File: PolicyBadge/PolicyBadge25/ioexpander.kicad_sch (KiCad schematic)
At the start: 25 parts, among them Q1 2N7002, U10 YX-SMD5020, U9 TCA9555PWR

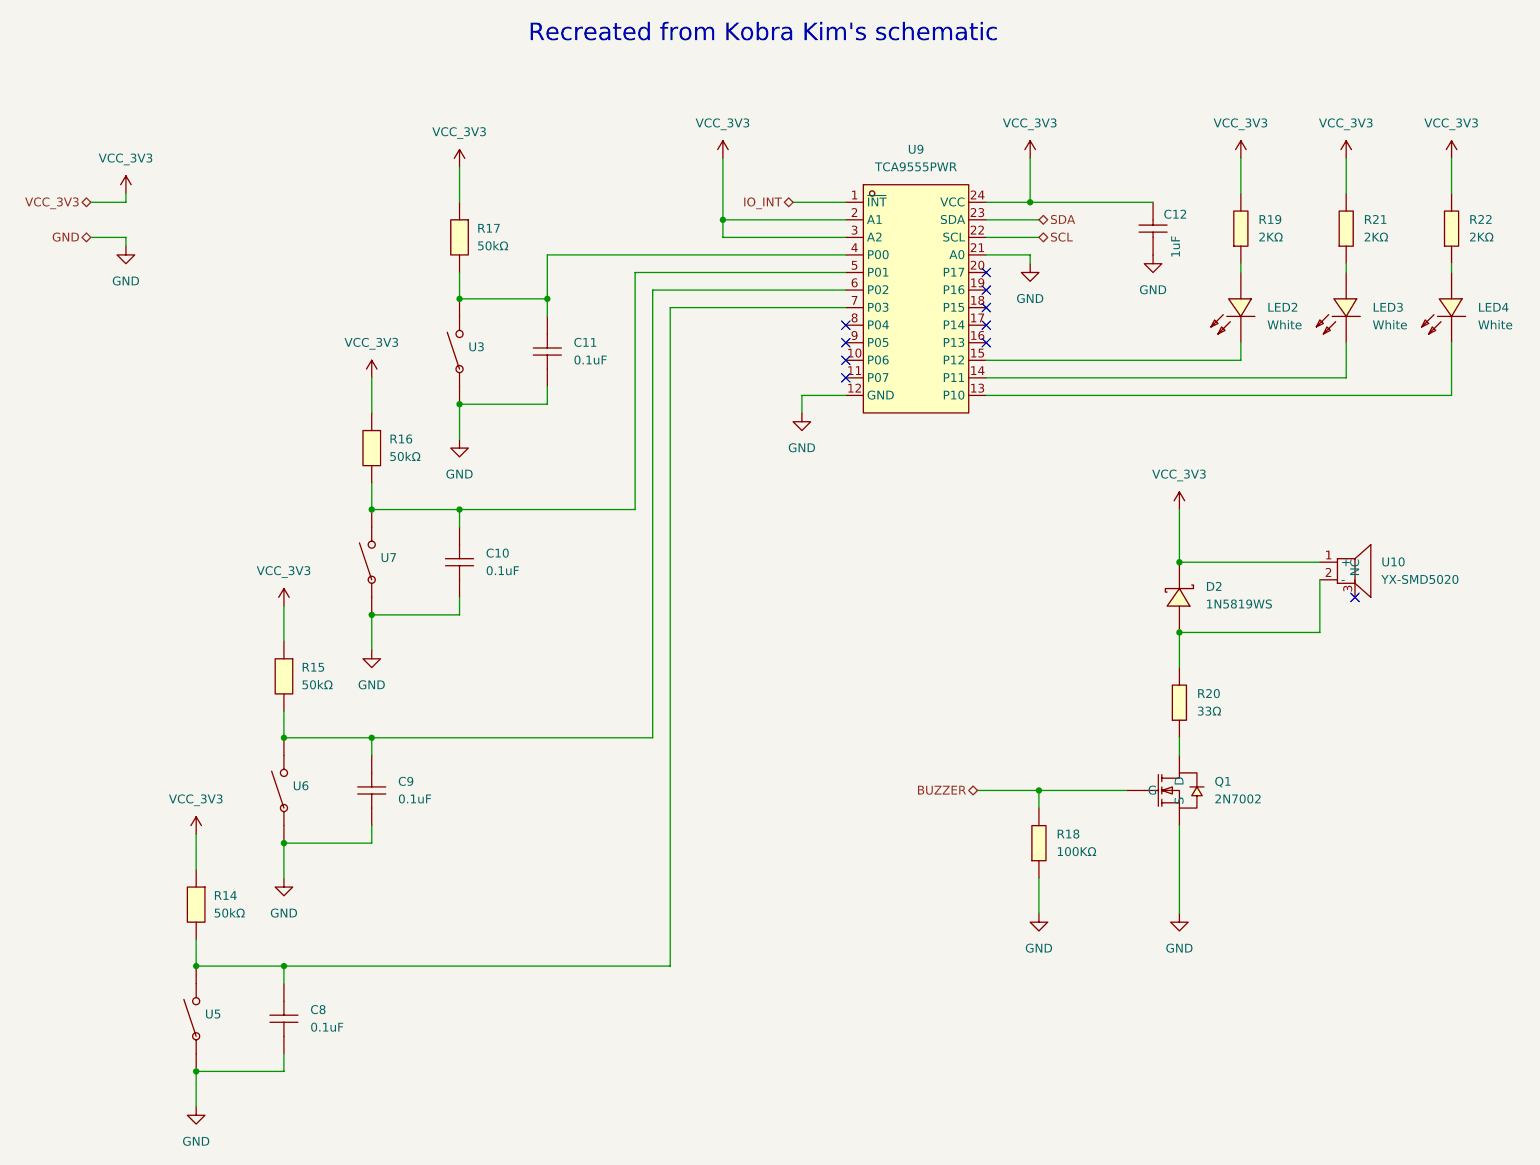
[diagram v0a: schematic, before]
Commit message: Lots of changes, laying out board for board shape
Updated switches
Added headers for XAIO
Fixed Batt Connector polarity
10K pullup on int
Batt monitor resistor divider
Fix buzzer trace
XAIO footprint spacing
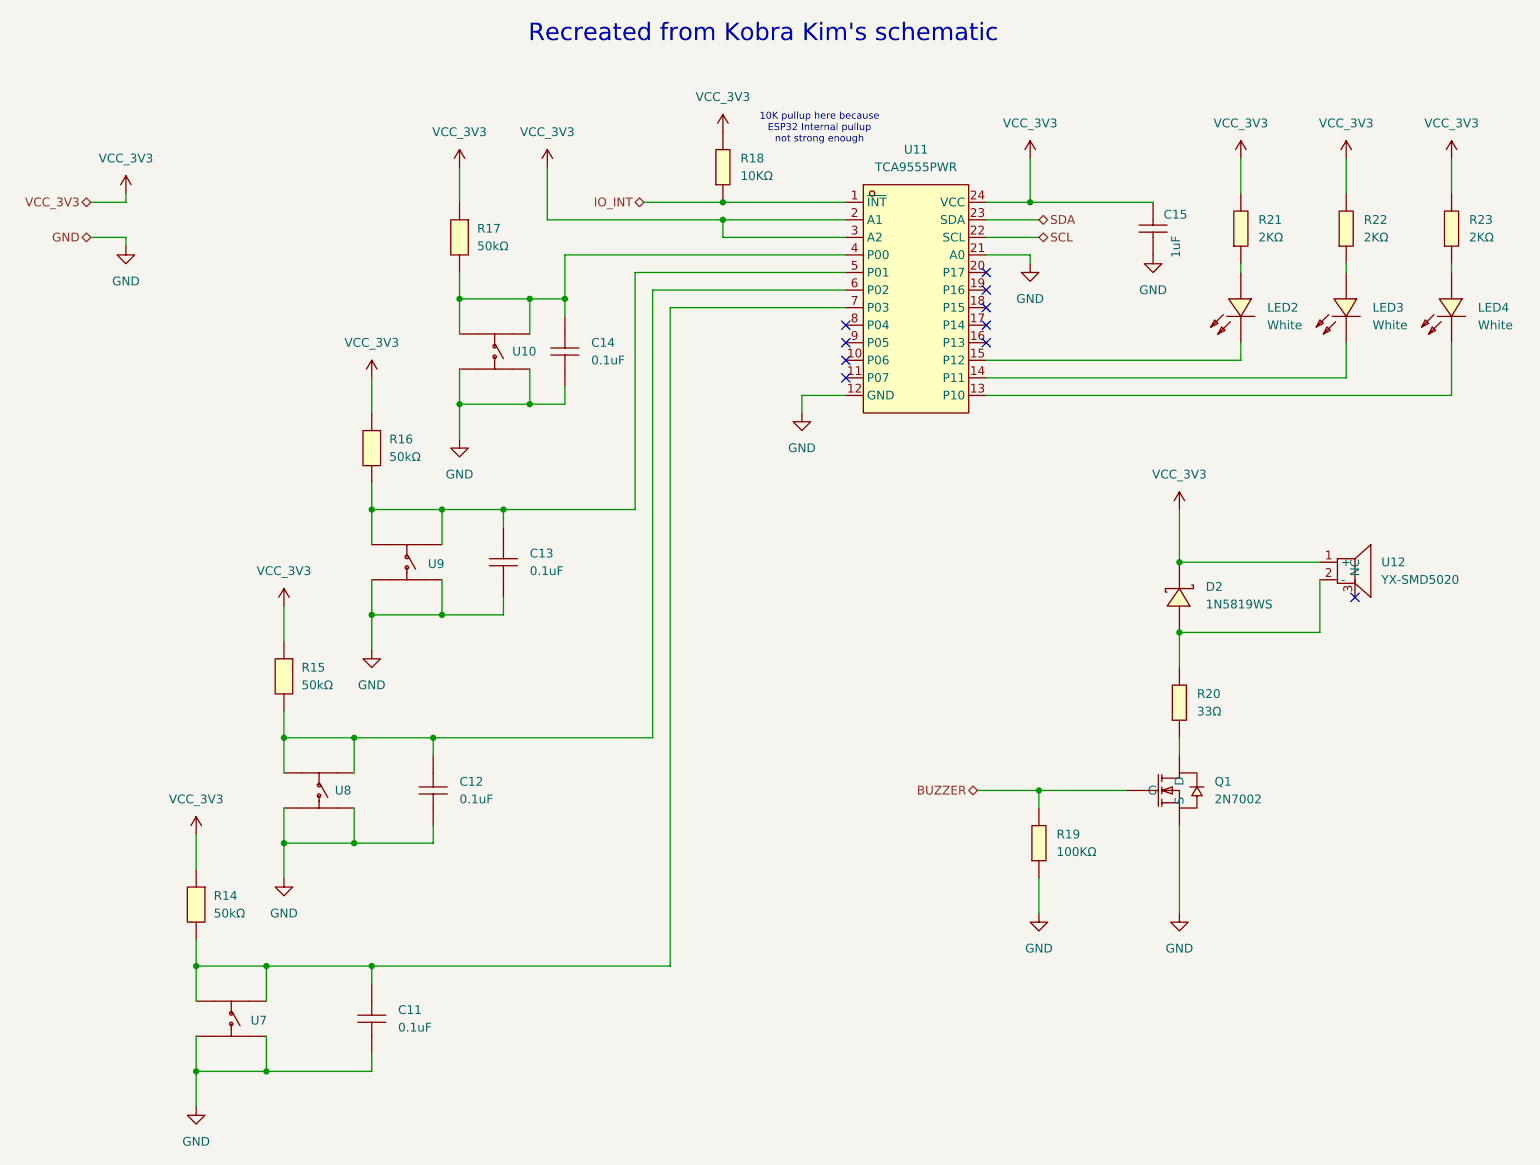
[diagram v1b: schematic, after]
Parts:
- removed U3, U5, U6, U7: ~, imported:SW-TH_HRO_K2-1109DF-EXXW-XX, symbol JLCPCB:K2-1109DF-E4SW-04
- added R18: 10KΩ, imported:R0603, symbol JLCPCB:0603WAF1002T5E
- added U10, U7, U8, U9: ~, imported:SW-SMD_4P-L6.0-W6.0-P4.50-LS9.2, symbol JLCPCB:TPS645-5NC60
- renumbered C8 to C11, C9 to C12, C10 to C13, C11 to C14, C12 to C15, R18 to R19, R19 to R21, R21 to R22, R22 to R23, U9 to U11, U10 to U12
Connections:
- net GND: now also U10.1, U10.2, U7.1, U7.2, U8.1, U8.2, U9.1, U9.2
- net IO_INT: now also R18.1
- net VCC_3V3: now also R18.2
- net at C12.2, R15.2, U11.6 (P02): now also U8.3, U8.4
- net at C14.2, R17.2, U11.4 (P00): now also U10.3, U10.4
- net at C13.2, R16.2, U11.5 (P01): now also U9.3, U9.4
- net at C11.2, R14.2, U11.7 (P03): now also U7.3, U7.4
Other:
- note added: "10K pullup here because ESP32 Internal pullup not strong enough"
- moved on the sheet: C11, C12, C13, C14
